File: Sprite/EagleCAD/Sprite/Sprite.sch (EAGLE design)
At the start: 29 parts, among them U1 CC430F5137, U2 HMC5883LSMD, U3 ITG-3200, X1 26 MHz

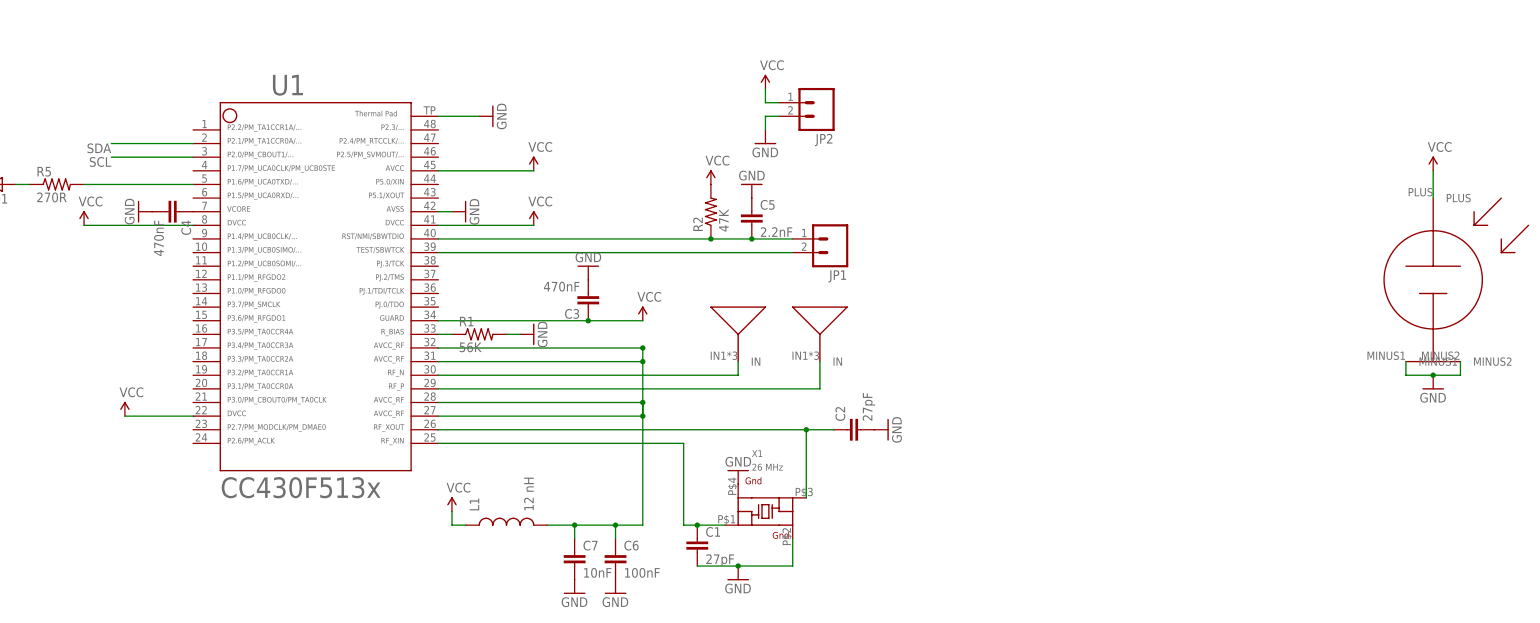
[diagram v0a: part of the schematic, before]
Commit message: Added back solar cells and TCXO to Sprite
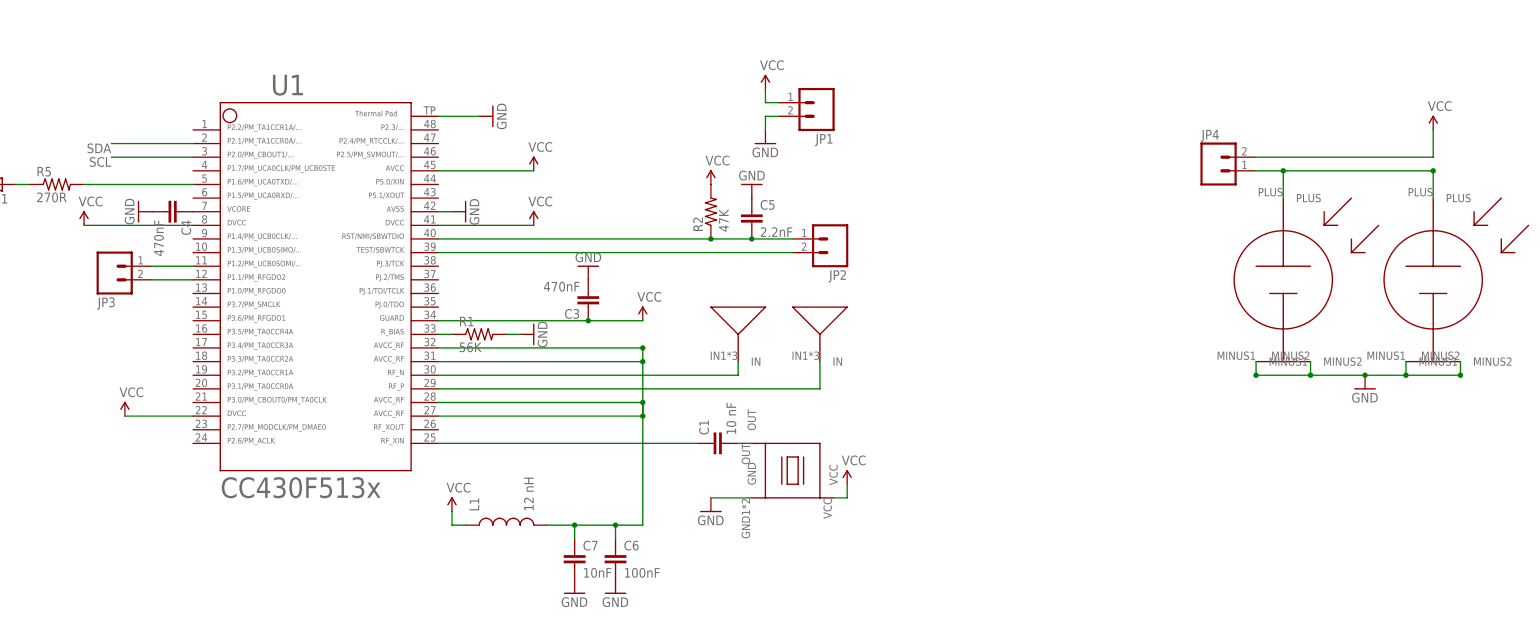
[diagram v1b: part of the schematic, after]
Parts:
- removed C2: 27pF, SparkFun:CAP0603-CAP
- removed X1: 26 MHz, ABM11:ABM11_CERAMIC_SMD_CRYSTALABM11
- added JP3, JP4: (no value), SparkFun:M02PTH
- added S2: TASC, TASC:TASC
- added U$1: TCXO_7Z, SpriteTCXO:TCXO_7Z
- C1: value 27pF -> 10 nF
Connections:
- removed net N$2: C1.1, U1.25, X1.P$1
- new net N$12: C1.2, U$1.OUT
- new net RXD: JP3.2, U1.12
- new net TXD: JP3.1, U1.11
- new net VSOLAR: JP4.1, S1.PLUS, S2.PLUS
- net GND: now also JP1.2, S2.MINUS1, S2.MINUS2, U$1.GND; no longer C1.2, C2.2, JP2.2, X1.GROUND2, X1.GROUND4
- net N$1: now also C1.1, U1.25; no longer C2.1, U1.26, X1.P$3
- net RST: now also JP2.1; no longer JP1.1
- net TEST: now also JP2.2; no longer JP1.2
- net VCC: now also JP1.1, JP4.2, U$1.VCC; no longer JP2.1, S1.PLUS
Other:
- moved on the sheet: C1, JP1, JP2

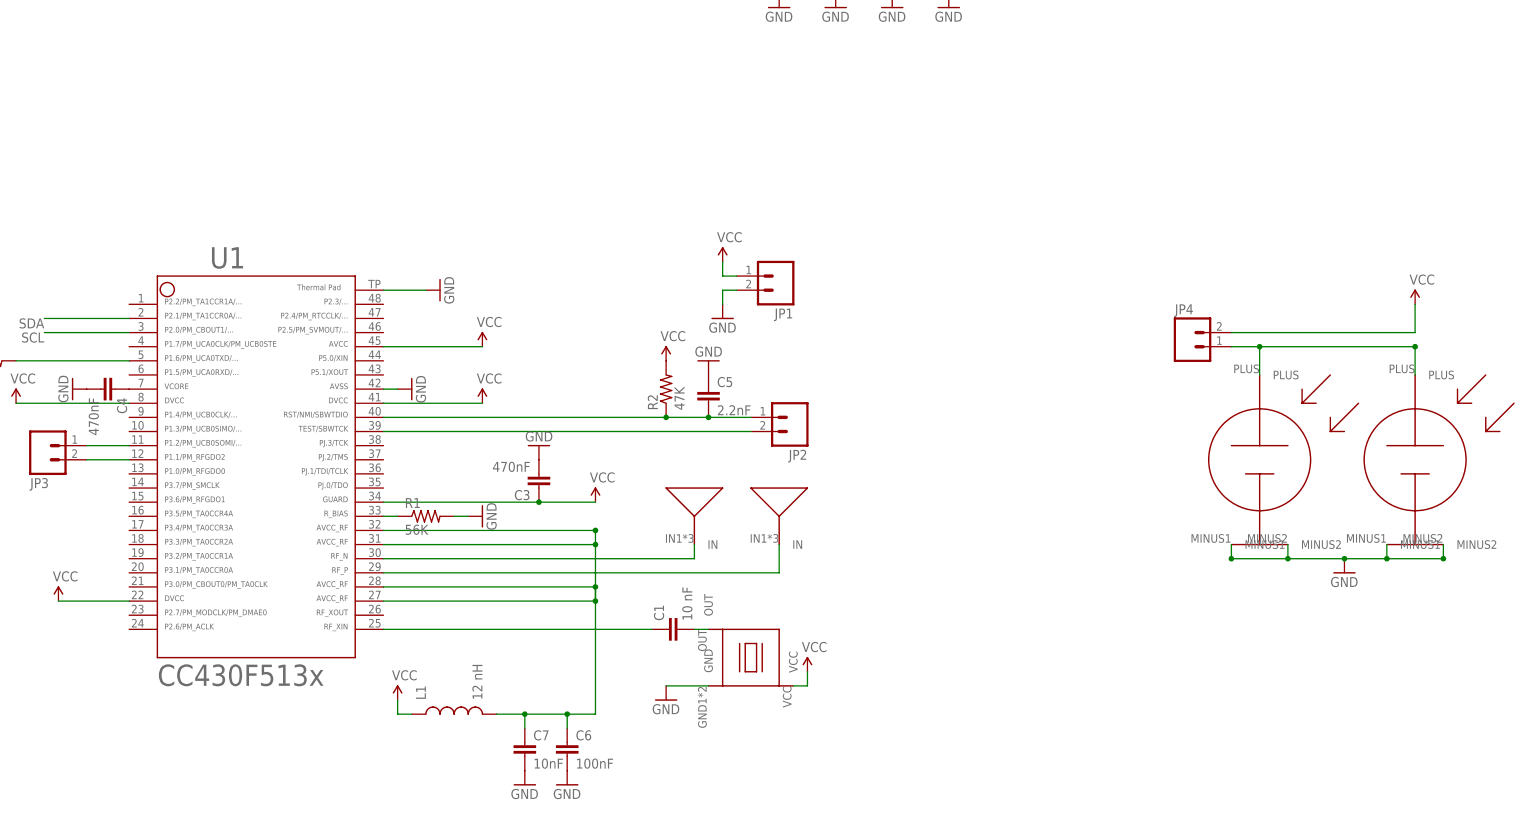
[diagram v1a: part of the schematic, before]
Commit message: New Sprite design
Several tweaks to the Sprite on the way to the flight unit. Added pins
and holes to interface to the deployer as well as a TCXO.
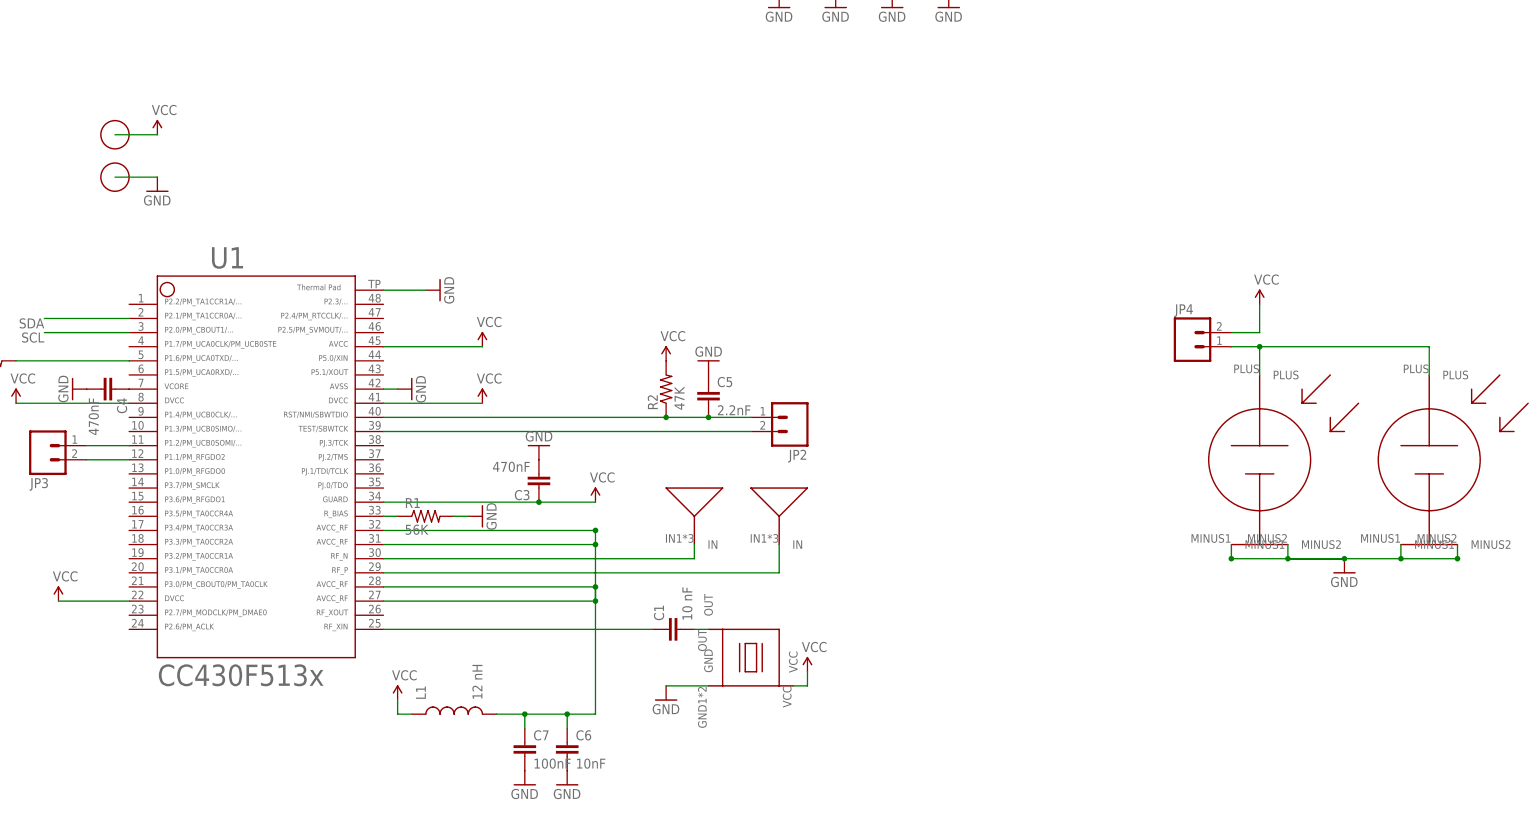
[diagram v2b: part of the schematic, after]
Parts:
- removed JP1: (no value), SparkFun:M02PTH
- added P1, P2: SPRITE_PIN, SpritePin:SPRITE_PIN
- C6: value 100nF -> 10nF
- C7: value 10nF -> 100nF
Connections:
- net GND: no longer JP1.2
- net VCC: no longer JP1.1
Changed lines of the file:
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@@
 <part name="GND21" library="SparkFun" deviceset="GND" device=""/>
 <part name="JP2" library="SparkFun" deviceset="M02" device="PTH"/>
-<part name="JP1" library="SparkFun" deviceset="M02" device="PTH"/>
 <part name="GND16" library="SparkFun" deviceset="GND" device=""/>
 <part name="P+4" library="SparkFun" deviceset="VCC" device=""/>
@@
 <part name="L1" library="SparkFun" deviceset="INDUCTOR" device="0603" value="12 nH"/>
 <part name="P+10" library="SparkFun" deviceset="VCC" device=""/>
-<part name="C7" library="SparkFun" deviceset="CAP" device="0603-CAP" value="10nF"/>
-<part name="C6" library="SparkFun" deviceset="CAP" device="0603-CAP" value="100nF"/>
+<part name="C7" library="SparkFun" deviceset="CAP" device="0603-CAP" value="100nF"/>
+<part name="C6" library="SparkFun" deviceset="CAP" device="0603-CAP" value="10nF"/>
 <part name="GND22" library="SparkFun" deviceset="GND" device=""/>
 <part name="GND23" library="SparkFun" deviceset="GND" device=""/>
-<part name="S1" library="TASC" deviceset="TASC" device=""/>
 <part name="LED1" library="SparkFun" deviceset="LED" device="0603"/>
 <part name="GND10" library="SparkFun" deviceset="GND" device=""/>
@@
 <part name="U$1" library="SpriteTCXO" deviceset="TCXO_7Z" device=""/>
 <part name="P+11" library="SparkFun" deviceset="VCC" device=""/>
+<part name="P2" library="SpritePin" deviceset="SPRITE_PIN" device=""/>
+<part name="P1" library="SpritePin" deviceset="SPRITE_PIN" device=""/>
+<part name="S1" library="TASC" deviceset="TASC" device=""/>
 </parts>
 <sheets>
@@
 <instances>
 <instance part="GND1" gate="1" x="347.98" y="66.04"/>
-<instance part="P+1" gate="1" x="360.68" y="114.3"/>
+<instance part="P+1" gate="1" x="332.74" y="114.3"/>
 <instance part="U1" gate="G$1" x="152.4" y="86.36"/>
 <instance part="C1" gate="G$1" x="228.6" y="55.88" rot="R90"/>
@@
 <instance part="GND21" gate="1" x="203.2" y="88.9" rot="R180"/>
 <instance part="JP2" gate="G$1" x="248.92" y="93.98" rot="R180"/>
-<instance part="JP1" gate="G$1" x="246.38" y="119.38" rot="R180"/>
-<instance part="GND16" gate="1" x="236.22" y="111.76"/>
-<instance part="P+4" gate="1" x="236.22" y="121.92"/>
+<instance part="GND16" gate="1" x="134.62" y="134.62"/>
+<instance part="P+4" gate="1" x="134.62" y="144.78"/>
 <instance part="ANT-N" gate="G$1" x="231.14" y="76.2"/>
 <instance part="ANT-P" gate="G$1" x="246.38" y="76.2"/>
@@
 <instance part="GND22" gate="1" x="200.66" y="27.94"/>
 <instance part="GND23" gate="1" x="208.28" y="27.94"/>
-<instance part="S1" gate="G$1" x="360.68" y="86.36"/>
 <instance part="LED1" gate="G$1" x="93.98" y="104.14" rot="R270"/>
 <instance part="GND10" gate="1" x="86.36" y="99.06"/>
@@
 <instance part="U$1" gate="G$1" x="241.3" y="50.8" rot="MR0"/>
 <instance part="P+11" gate="1" x="251.46" y="48.26"/>
+<instance part="P2" gate="G$1" x="127" y="144.78"/>
+<instance part="P1" gate="G$1" x="127" y="137.16"/>
+<instance part="S1" gate="G$1" x="363.22" y="86.36"/>
 </instances>
 <busses>
@@
 </segment>
 <segment>
-<pinref part="JP1" gate="G$1" pin="1"/>
-<pinref part="P+4" gate="1" pin="VCC"/>
-<wire x1="238.76" y1="119.38" x2="236.22" y2="119.38" width="0.1524" layer="91"/>
-<wire x1="236.22" y1="119.38" x2="236.22" y2="121.92" width="0.1524" layer="91"/>
-</segment>
-<segment>
 <pinref part="R2" gate="G$1" pin="2"/>
 <pinref part="P+5" gate="1" pin="VCC"/>
@@
 <pinref part="JP4" gate="G$1" pin="2"/>
 <pinref part="P+1" gate="1" pin="VCC"/>
-<wire x1="327.66" y1="109.22" x2="360.68" y2="109.22" width="0.1524" layer="91"/>
-<wire x1="360.68" y1="109.22" x2="360.68" y2="114.3" width="0.1524" layer="91"/>
+<wire x1="327.66" y1="109.22" x2="332.74" y2="109.22" width="0.1524" layer="91"/>
+<wire x1="332.74" y1="109.22" x2="332.74" y2="114.3" width="0.1524" layer="91"/>
 </segment>
 <segment>
@@
 <wire x1="248.92" y1="45.72" x2="251.46" y2="45.72" width="0.1524" layer="91"/>
 <wire x1="251.46" y1="45.72" x2="251.46" y2="48.26" width="0.1524" layer="91"/>
+</segment>
+<segment>
+<pinref part="P+4" gate="1" pin="VCC"/>
+<wire x1="134.62" y1="144.78" x2="127" y2="144.78" width="0.1524" layer="91"/>
 </segment>
 </net>
@@
 </segment>
 <segment>
-<pinref part="JP1" gate="G$1" pin="2"/>
-<pinref part="GND16" gate="1" pin="GND"/>
-<wire x1="238.76" y1="116.84" x2="236.22" y2="116.84" width="0.1524" layer="91"/>
-<wire x1="236.22" y1="116.84" x2="236.22" y2="114.3" width="0.1524" layer="91"/>
-</segment>
-<segment>
 <pinref part="C5" gate="G$1" pin="1"/>
 <pinref part="GND2" gate="1" pin="GND"/>
@@
 </segment>
 <segment>
-<wire x1="355.6" y1="68.58" x2="355.6" y2="71.12" width="0.1524" layer="91"/>
-<pinref part="S1" gate="G$1" pin="MINUS1"/>
+<pinref part="U$1" gate="G$1" pin="GND"/>
+<pinref part="GND8" gate="1" pin="GND"/>
+<wire x1="226.06" y1="45.72" x2="233.68" y2="45.72" width="0.1524" layer="91"/>
+</segment>
+<segment>
 <pinref part="S2" gate="G$1" pin="MINUS1"/>
 <wire x1="327.66" y1="71.12" x2="327.66" y2="68.58" width="0.1524" layer="91"/>
 <pinref part="S2" gate="G$1" pin="MINUS2"/>
-<wire x1="327.66" y1="68.58" x2="337.82" y2="68.58" width="0.1524" layer="91"/>
+<wire x1="327.66" y1="68.58" x2="347.98" y2="68.58" width="0.1524" layer="91"/>
+<wire x1="347.98" y1="68.58" x2="337.82" y2="68.58" width="0.1524" layer="91"/>
 <wire x1="337.82" y1="68.58" x2="337.82" y2="71.12" width="0.1524" layer="91"/>
-<wire x1="337.82" y1="68.58" x2="347.98" y2="68.58" width="0.1524" layer="91"/>
+<junction x="327.66" y="68.58"/>
 <pinref part="GND1" gate="1" pin="GND"/>
-<wire x1="347.98" y1="68.58" x2="355.6" y2="68.58" width="0.1524" layer="91"/>
 <junction x="347.98" y="68.58"/>
+<junction x="337.82" y="68.58"/>
 <pinref part="S1" gate="G$1" pin="MINUS2"/>
-<wire x1="365.76" y1="68.58" x2="365.76" y2="71.12" width="0.1524" layer="91"/>
-<wire x1="365.76" y1="68.58" x2="355.6" y2="68.58" width="0.1524" layer="91"/>
-<junction x="327.66" y="68.58"/>
-<junction x="337.82" y="68.58"/>
-<junction x="355.6" y="68.58"/>
-<junction x="365.76" y="68.58"/>
-</segment>
-<segment>
-<pinref part="U$1" gate="G$1" pin="GND"/>
-<pinref part="GND8" gate="1" pin="GND"/>
-<wire x1="226.06" y1="45.72" x2="233.68" y2="45.72" width="0.1524" layer="91"/>
+<wire x1="368.3" y1="71.12" x2="368.3" y2="68.58" width="0.1524" layer="91"/>
+<pinref part="S1" gate="G$1" pin="MINUS1"/>
+<wire x1="358.14" y1="71.12" x2="358.14" y2="68.58" width="0.1524" layer="91"/>
+<wire x1="368.3" y1="68.58" x2="358.14" y2="68.58" width="0.1524" layer="91"/>
+<wire x1="358.14" y1="68.58" x2="337.82" y2="68.58" width="0.1524" layer="91"/>
+<junction x="358.14" y="68.58"/>
+<junction x="368.3" y="68.58"/>
+</segment>
+<segment>
+<pinref part="GND16" gate="1" pin="GND"/>
+<wire x1="134.62" y1="137.16" x2="127" y2="137.16" width="0.1524" layer="91"/>
 </segment>
 </net>
@@
 <segment>
 <pinref part="JP4" gate="G$1" pin="1"/>
-<pinref part="S1" gate="G$1" pin="PLUS"/>
 <wire x1="327.66" y1="106.68" x2="332.74" y2="106.68" width="0.1524" layer="91"/>
-<wire x1="332.74" y1="106.68" x2="360.68" y2="106.68" width="0.1524" layer="91"/>
-<wire x1="360.68" y1="106.68" x2="360.68" y2="101.6" width="0.1524" layer="91"/>
 <pinref part="S2" gate="G$1" pin="PLUS"/>
 <wire x1="332.74" y1="101.6" x2="332.74" y2="106.68" width="0.1524" layer="91"/>
+<pinref part="S1" gate="G$1" pin="PLUS"/>
+<wire x1="363.22" y1="101.6" x2="363.22" y2="106.68" width="0.1524" layer="91"/>
+<wire x1="363.22" y1="106.68" x2="332.74" y2="106.68" width="0.1524" layer="91"/>
 <junction x="332.74" y="106.68"/>
-<junction x="360.68" y="106.68"/>
-</segment>
-</net>
+</segment>
+</net>
